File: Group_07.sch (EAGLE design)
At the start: 29 parts, among them J1 POWER_JACKPTH_LOCK, U1 +12v, U3 TCA9546ASO16, U4 TMUX1208

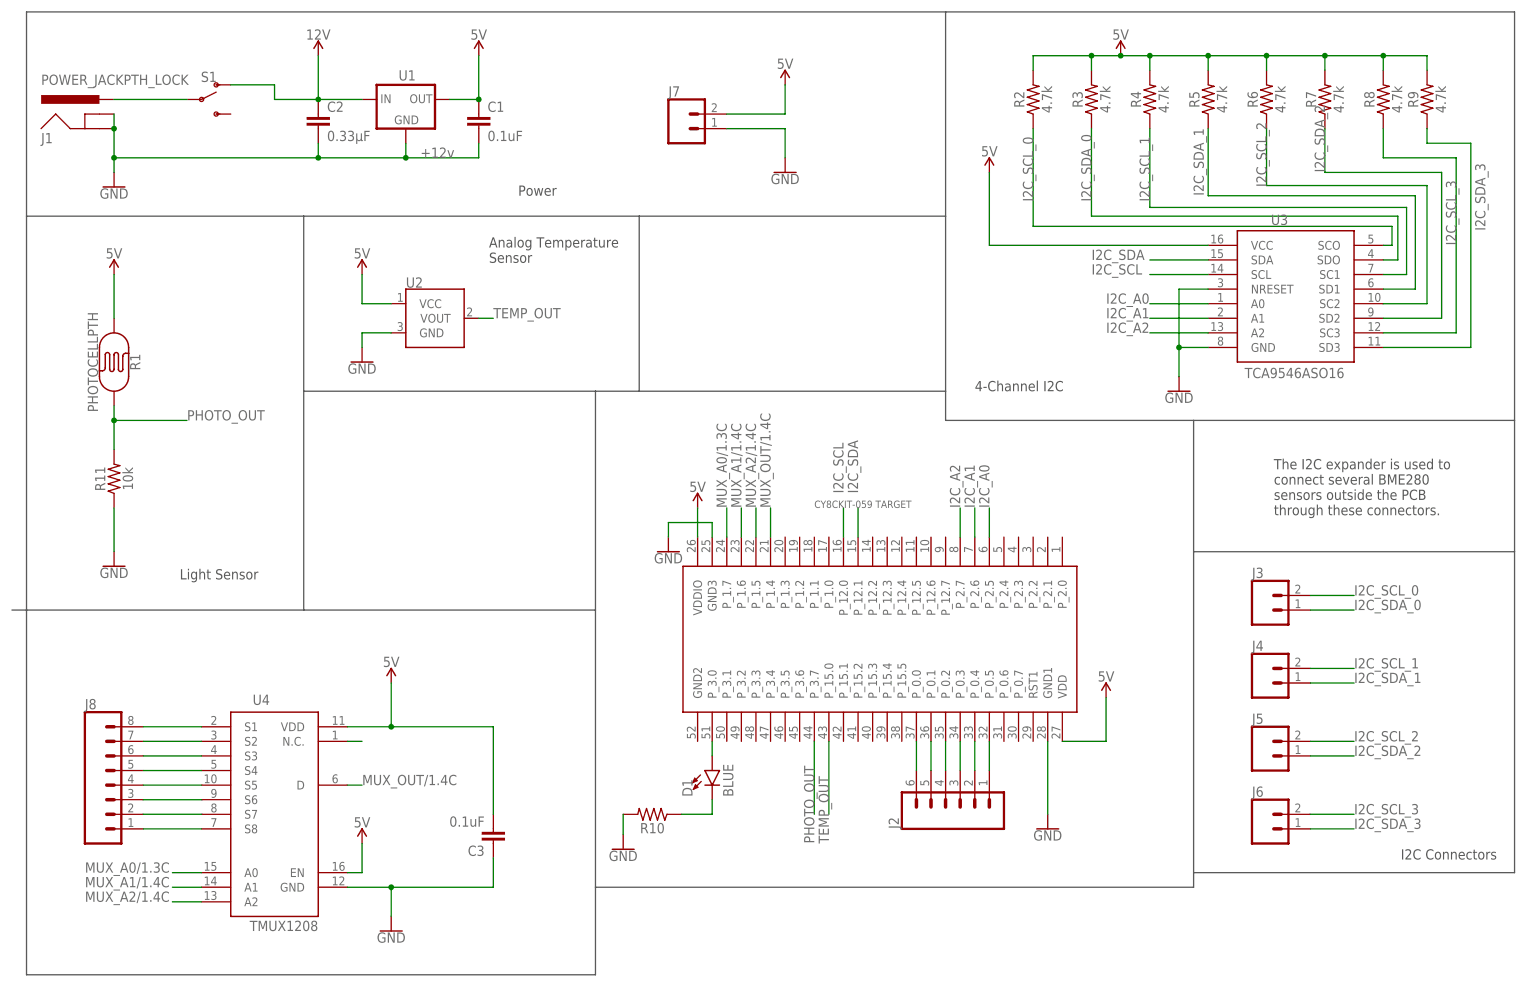
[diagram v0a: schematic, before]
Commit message: Correction in the schematic
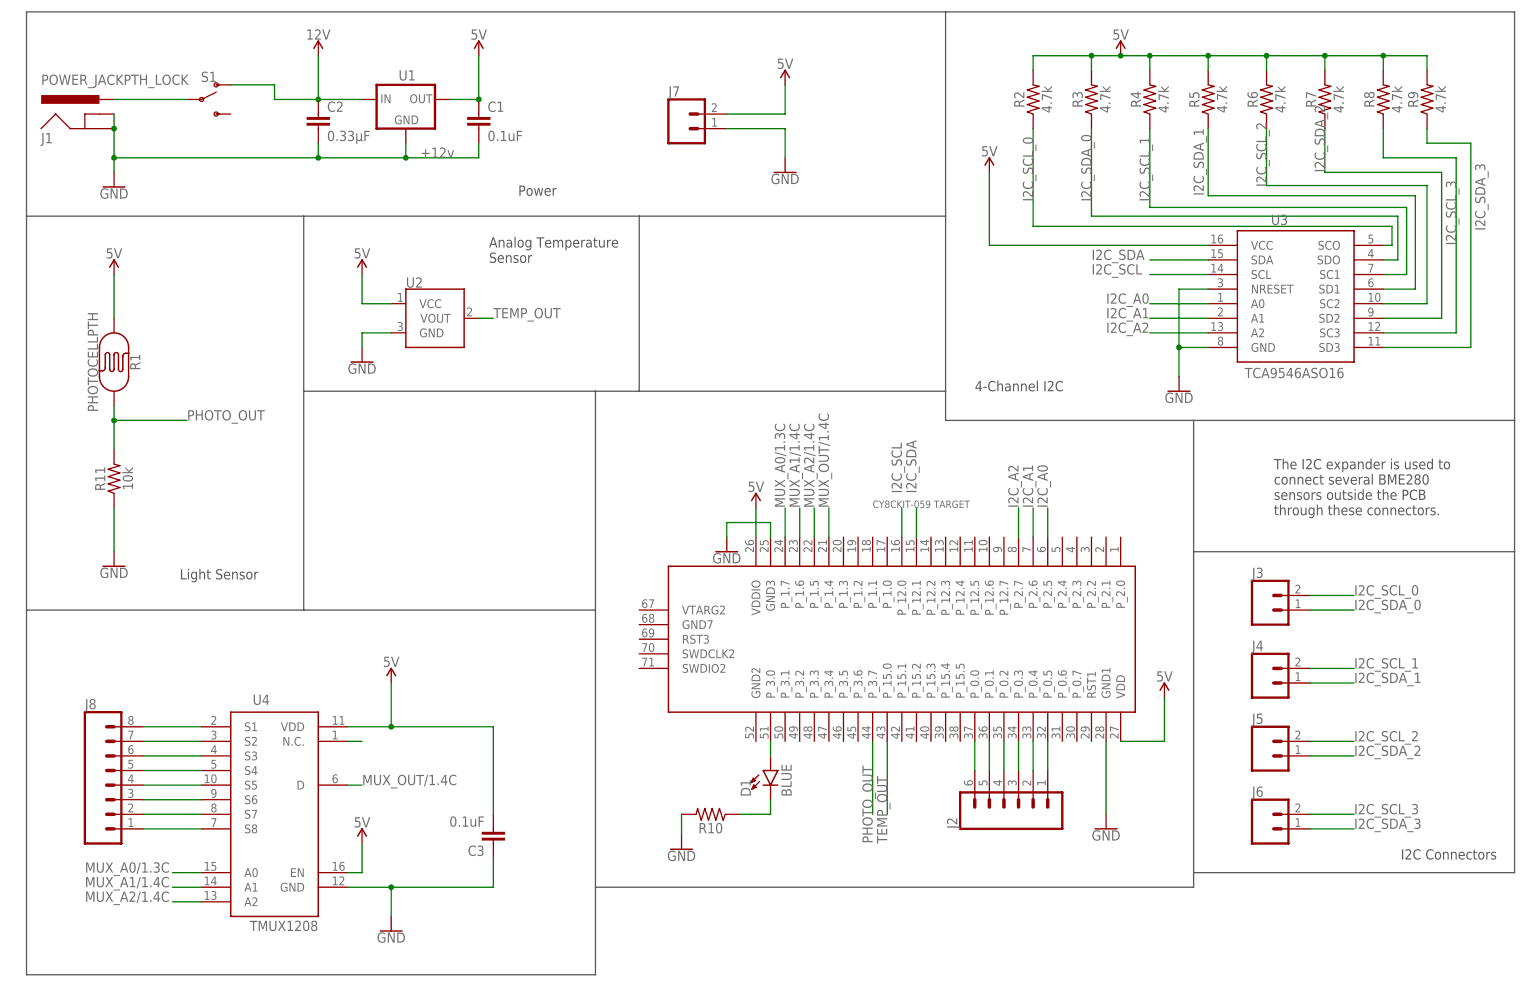
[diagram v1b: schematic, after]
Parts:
- removed U$4: CY8CKIT-059_TARGET_3, CY8KIT-059:CY8CKIT-059_TARGET_3
- added U$1: CY8CKIT-059_TARGET, CYKIT:CY8CKIT-059_TARGET
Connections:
- net 5V: now also U$1.VDD; no longer U$4.VDD
- net GND: now also U$1.GND3; no longer U$4.GND3
- net I2C_A0: now also U$1.P_2.5; no longer U$4.P_2.5
- net I2C_A1: now also U$1.P_2.6; no longer U$4.P_2.6
- net I2C_A2: now also U$1.P_2.7; no longer U$4.P_2.7
- net I2C_SCL: now also U$1.P_12.0; no longer U$4.P_12.0
- net I2C_SDA: now also U$1.P_12.1; no longer U$4.P_12.1
- net MUX_A0/1.3C: now also U$1.P_1.7; no longer U$4.P_1.7
- net MUX_A1/1.4C: now also U$1.P_1.6; no longer U$4.P_1.6
- net MUX_A2/1.4C: now also U$1.P_1.5; no longer U$4.P_1.5
- net MUX_OUT/1.4C: now also U$1.P_1.4; no longer U$4.P_1.4
- net N$18: now also U$1.VDDIO; no longer U$4.VDDIO
- net N$20: now also U$1.GND1; no longer U$4.GND1
- net N$3: now also U$1.P_0.0; no longer U$4.P_0.0
- net N$4: now also U$1.P_0.1; no longer U$4.P_0.1
- net N$5: now also U$1.P_0.2; no longer U$4.P_0.2
- net N$6: now also U$1.P_0.3; no longer U$4.P_0.3
- net N$7: now also U$1.P_0.4; no longer U$4.P_0.4
- net N$8: now also U$1.P_0.5; no longer U$4.P_0.5
- net N$9: now also U$1.P_3.0; no longer U$4.P_3.0
- net PHOTO_OUT: now also U$1.P_3.7; no longer U$4.P_3.7
- net TEMP_OUT: now also U$1.P_15.0; no longer U$4.P_15.0
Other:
- moved on the sheet: D1, J2, R10

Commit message: Silkscreen
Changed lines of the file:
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@@
 <attribute name="VALUE" x="59.944" y="155.321" size="1.778" layer="96" font="vector"/>
 </instance>
-<instance part="C1" gate="G$1" x="86.36" y="157.48" smashed="yes">
-<attribute name="NAME" x="87.884" y="160.401" size="1.778" layer="95" font="vector"/>
-<attribute name="VALUE" x="87.884" y="155.321" size="1.778" layer="96" font="vector"/>
+<instance part="C1" gate="G$1" x="86.36" y="157.226" smashed="yes">
+<attribute name="NAME" x="87.884" y="160.147" size="1.778" layer="95" font="vector"/>
+<attribute name="VALUE" x="87.884" y="155.067" size="1.778" layer="96" font="vector"/>
 </instance>
 <instance part="U1" gate="G$1" x="73.66" y="162.56" smashed="yes">
 <attribute name="NAME" x="72.39" y="165.862" size="1.778" layer="95"/>
-<attribute name="VALUE" x="76.2" y="152.4" size="1.778" layer="96"/>
+<attribute name="VALUE" x="71.374" y="155.194" size="1.778" layer="96"/>
 </instance>
 <instance part="J7" gate="G$1" x="121.92" y="157.48" smashed="yes">
@@
 <nets>
 <net name="5V" class="0">
-<segment>
-<pinref part="SUPPLY4" gate="G$1" pin="5V"/>
-<pinref part="C1" gate="G$1" pin="1"/>
-<wire x1="86.36" y1="170.18" x2="86.36" y2="162.56" width="0.1524" layer="91"/>
-<pinref part="U1" gate="G$1" pin="OUT"/>
-<wire x1="81.28" y1="162.56" x2="86.36" y2="162.56" width="0.1524" layer="91"/>
-<junction x="86.36" y="162.56"/>
-</segment>
 <segment>
 <pinref part="J7" gate="G$1" pin="2"/>
@@
 <pinref part="U4" gate="G$1" pin="VDD"/>
 </segment>
+<segment>
+<pinref part="U1" gate="G$1" pin="OUT"/>
+<wire x1="81.28" y1="162.56" x2="84.328" y2="162.56" width="0.1524" layer="91"/>
+<wire x1="84.328" y1="162.56" x2="84.328" y2="162.814" width="0.1524" layer="91"/>
+<pinref part="C1" gate="G$1" pin="1"/>
+<wire x1="84.328" y1="162.814" x2="86.36" y2="162.814" width="0.1524" layer="91"/>
+<wire x1="86.36" y1="162.814" x2="86.36" y2="162.306" width="0.1524" layer="91"/>
+<pinref part="SUPPLY4" gate="G$1" pin="5V"/>
+<wire x1="86.36" y1="162.306" x2="86.36" y2="170.18" width="0.1524" layer="91"/>
+<junction x="86.36" y="162.306"/>
+</segment>
 </net>
 <net name="N$1" class="0">
@@
 <pinref part="C1" gate="G$1" pin="2"/>
 <wire x1="73.66" y1="152.4" x2="86.36" y2="152.4" width="0.1524" layer="91"/>
-<wire x1="86.36" y1="152.4" x2="86.36" y2="154.94" width="0.1524" layer="91"/>
+<wire x1="86.36" y1="152.4" x2="86.36" y2="154.686" width="0.1524" layer="91"/>
 <junction x="73.66" y="152.4"/>
 </segment>

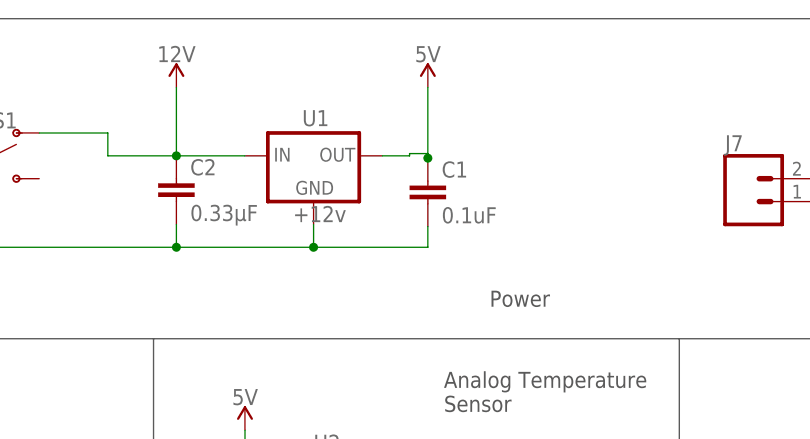
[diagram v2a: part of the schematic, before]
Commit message: Modifica silkscreen, mask and DRC check
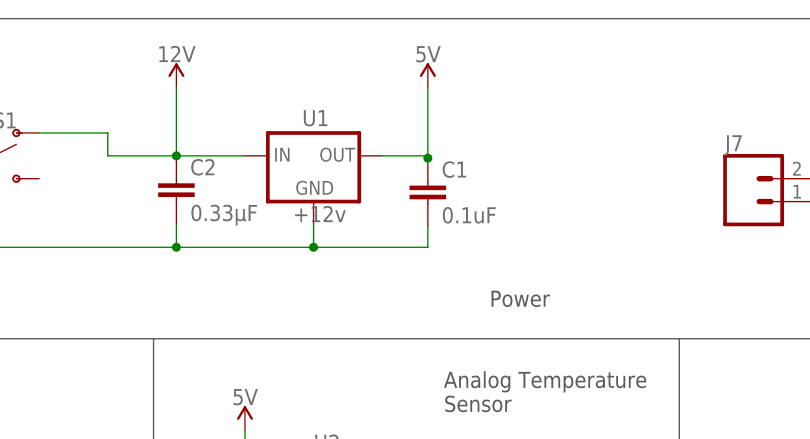
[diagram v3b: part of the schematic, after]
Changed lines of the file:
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@@
 <segment>
 <pinref part="U1" gate="G$1" pin="OUT"/>
-<wire x1="81.28" y1="162.56" x2="84.328" y2="162.56" width="0.1524" layer="91"/>
-<wire x1="84.328" y1="162.56" x2="84.328" y2="162.814" width="0.1524" layer="91"/>
+<wire x1="81.28" y1="162.56" x2="86.36" y2="162.56" width="0.1524" layer="91"/>
 <pinref part="C1" gate="G$1" pin="1"/>
-<wire x1="84.328" y1="162.814" x2="86.36" y2="162.814" width="0.1524" layer="91"/>
-<wire x1="86.36" y1="162.814" x2="86.36" y2="162.306" width="0.1524" layer="91"/>
+<wire x1="86.36" y1="162.56" x2="86.36" y2="162.306" width="0.1524" layer="91"/>
 <pinref part="SUPPLY4" gate="G$1" pin="5V"/>
 <wire x1="86.36" y1="162.306" x2="86.36" y2="170.18" width="0.1524" layer="91"/>
